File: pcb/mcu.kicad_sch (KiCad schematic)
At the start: 24 parts, among them SW1 PTS815, SW3 PTS815, U8 STM32H523VETx, Y1 ECS-160-12-33B2Q-JES-TR3, Y2 SC32S-7PF20PPM

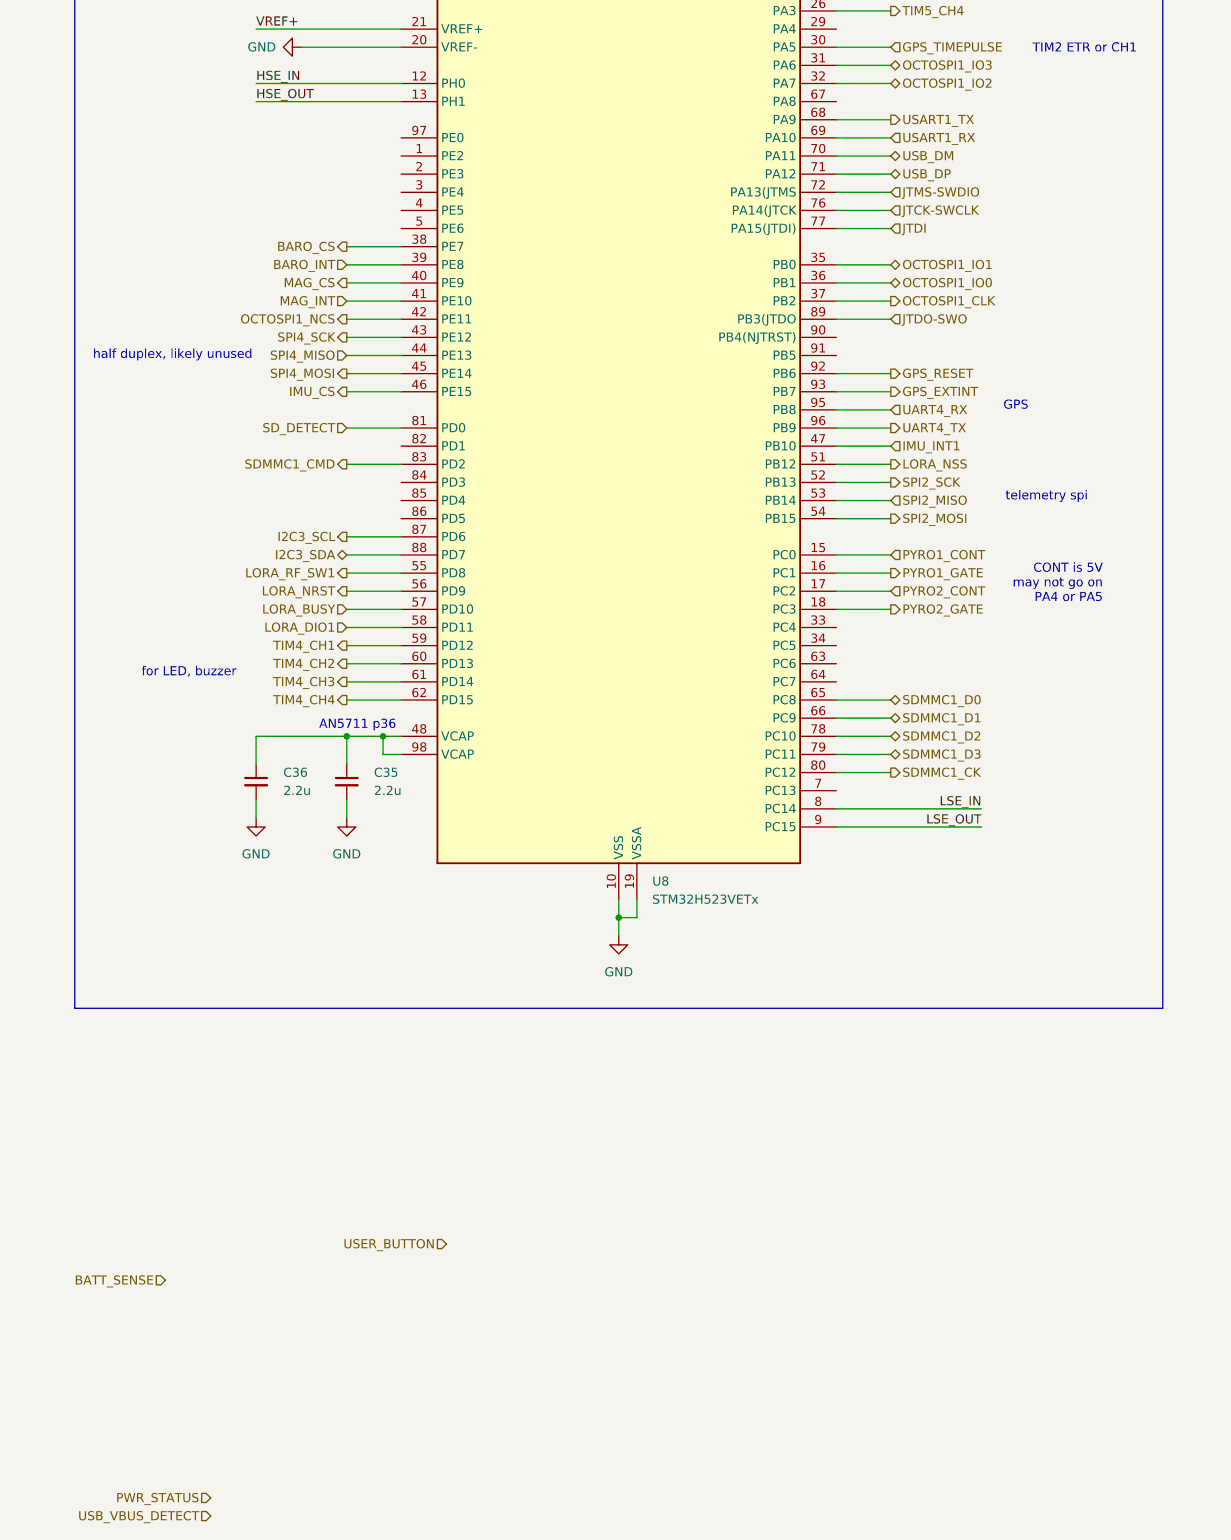
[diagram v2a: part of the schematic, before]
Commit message: Shuffle pins to allow for additional I2C
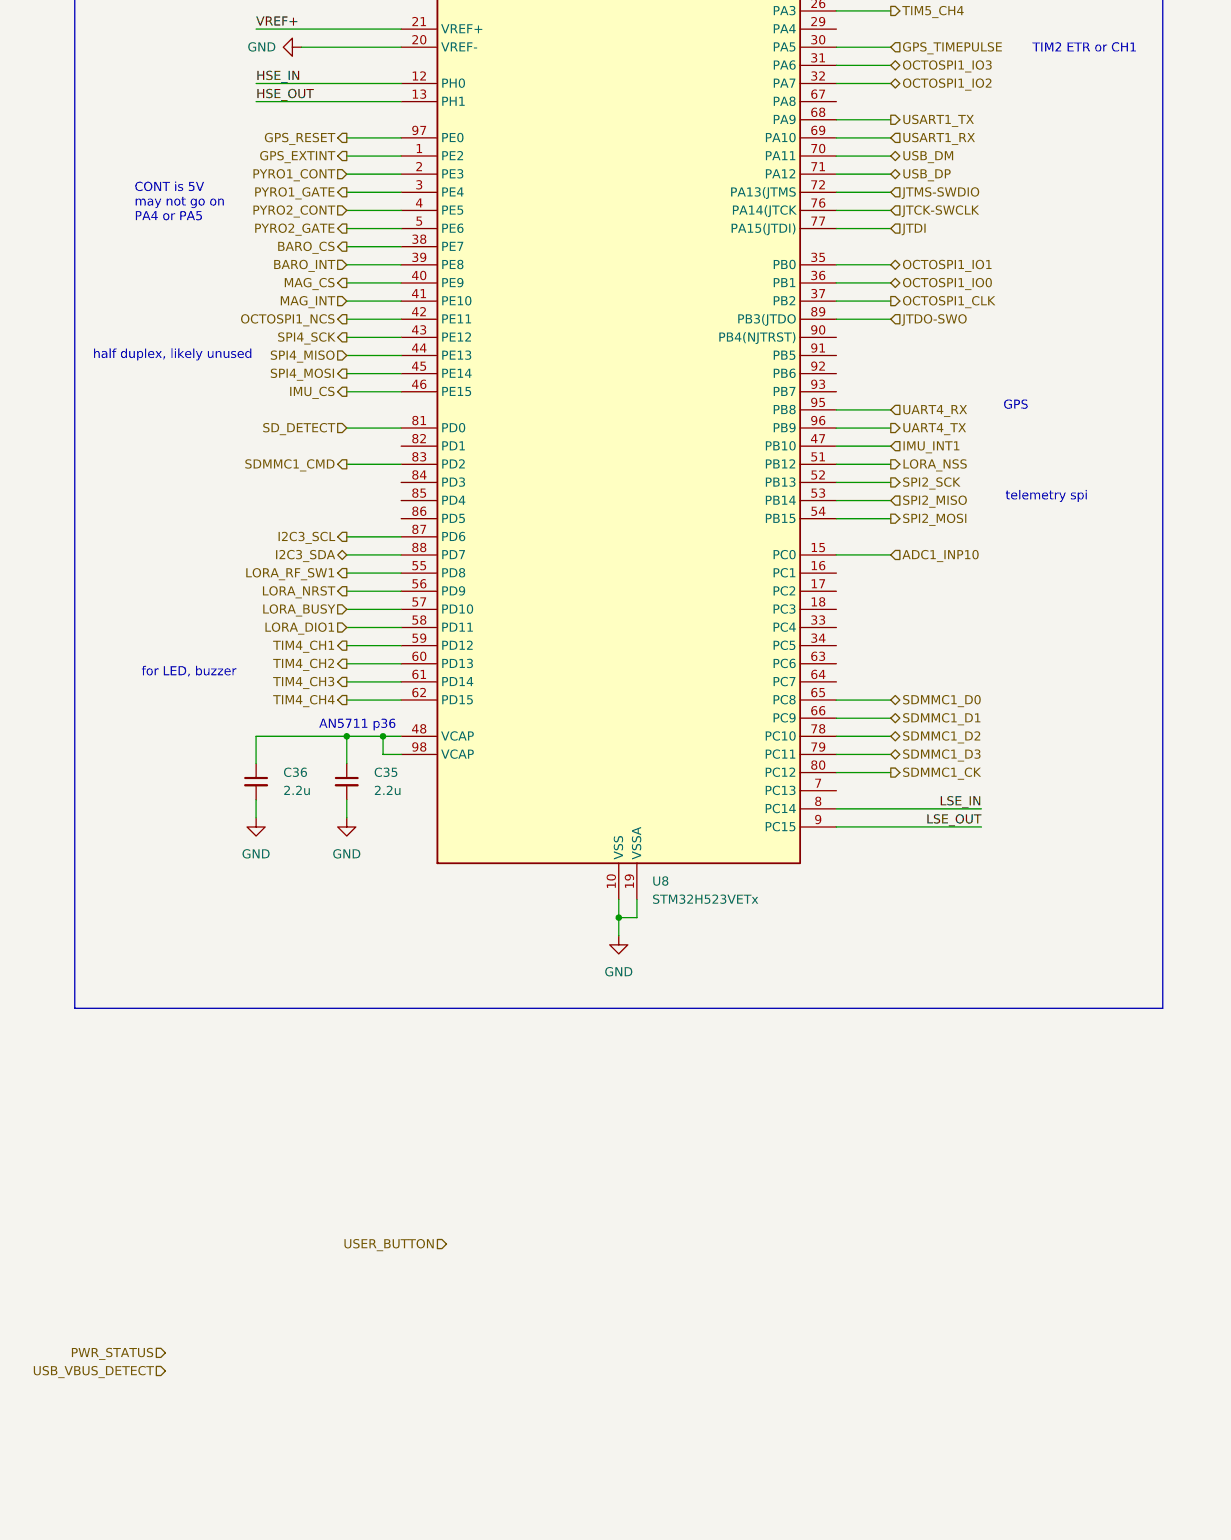
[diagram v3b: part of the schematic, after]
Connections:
- net GPS_EXTINT: now also U8.1 (PE2); no longer U8.93 (PB7)
- net GPS_RESET: now also U8.97 (PE0); no longer U8.92 (PB6)
- net PYRO1_CONT: now also U8.2 (PE3); no longer U8.15 (PC0)
- net PYRO1_GATE: now also U8.3 (PE4); no longer U8.16 (PC1)
- net PYRO2_CONT: now also U8.4 (PE5); no longer U8.17 (PC2)
- net PYRO2_GATE: now also U8.5 (PE6); no longer U8.18 (PC3)
- new net ADC1_INP10: U8.15 (PC0)

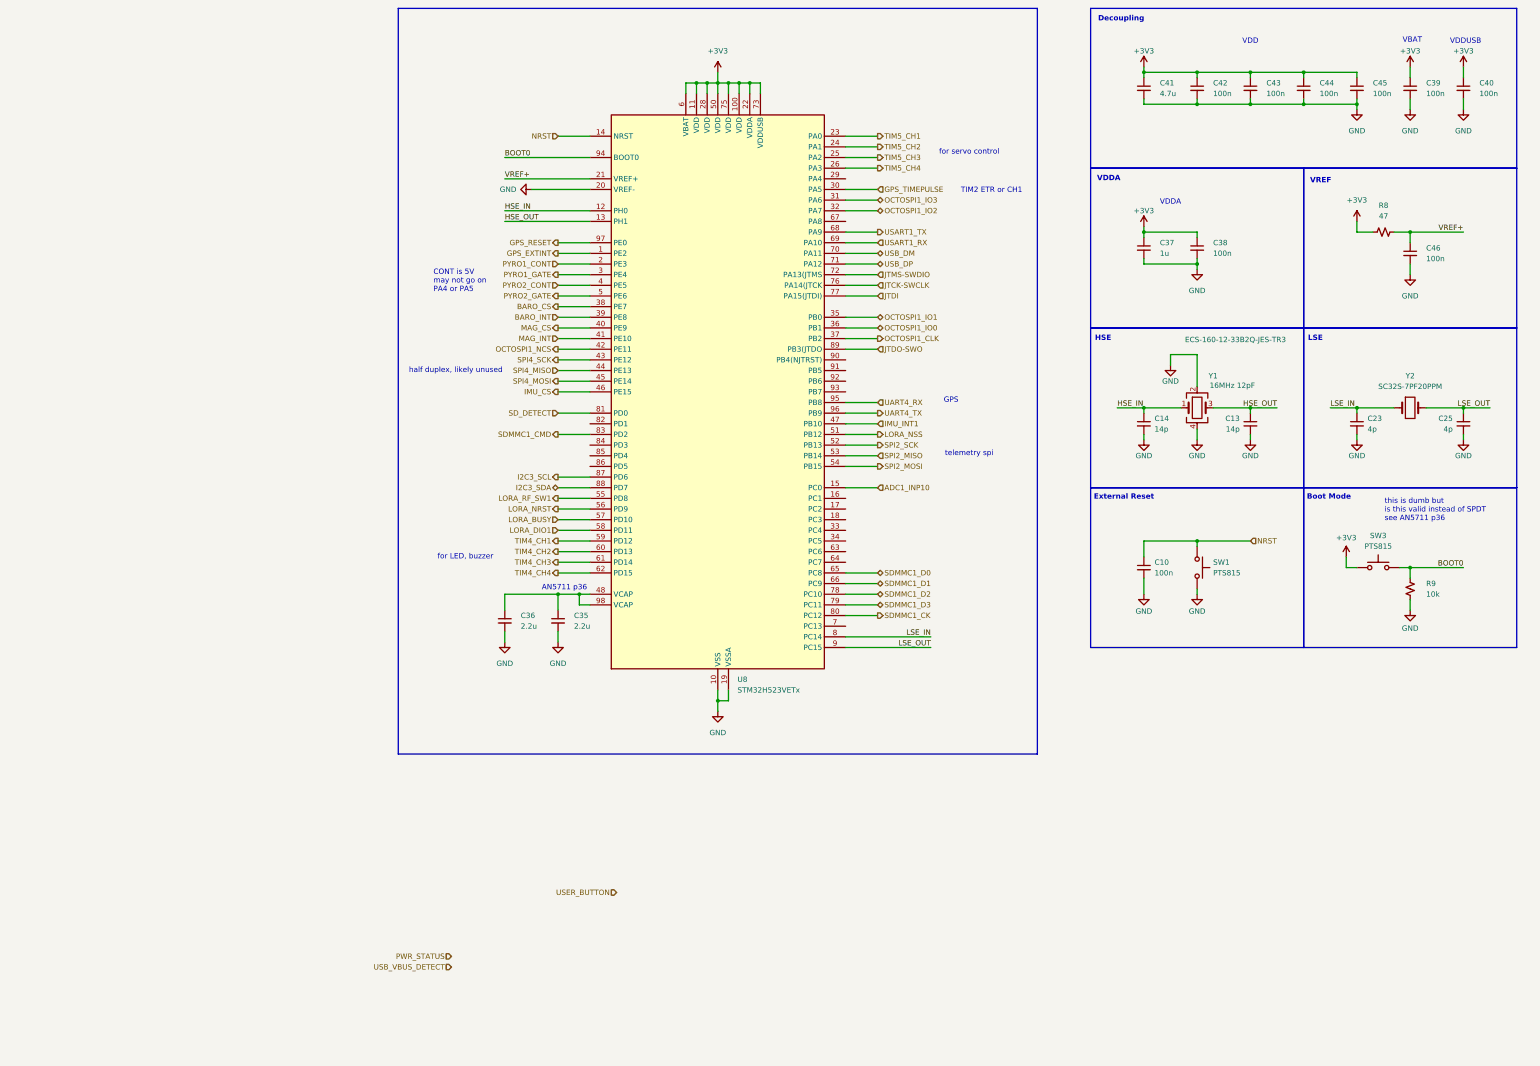
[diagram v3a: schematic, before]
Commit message: Fix pin directionality
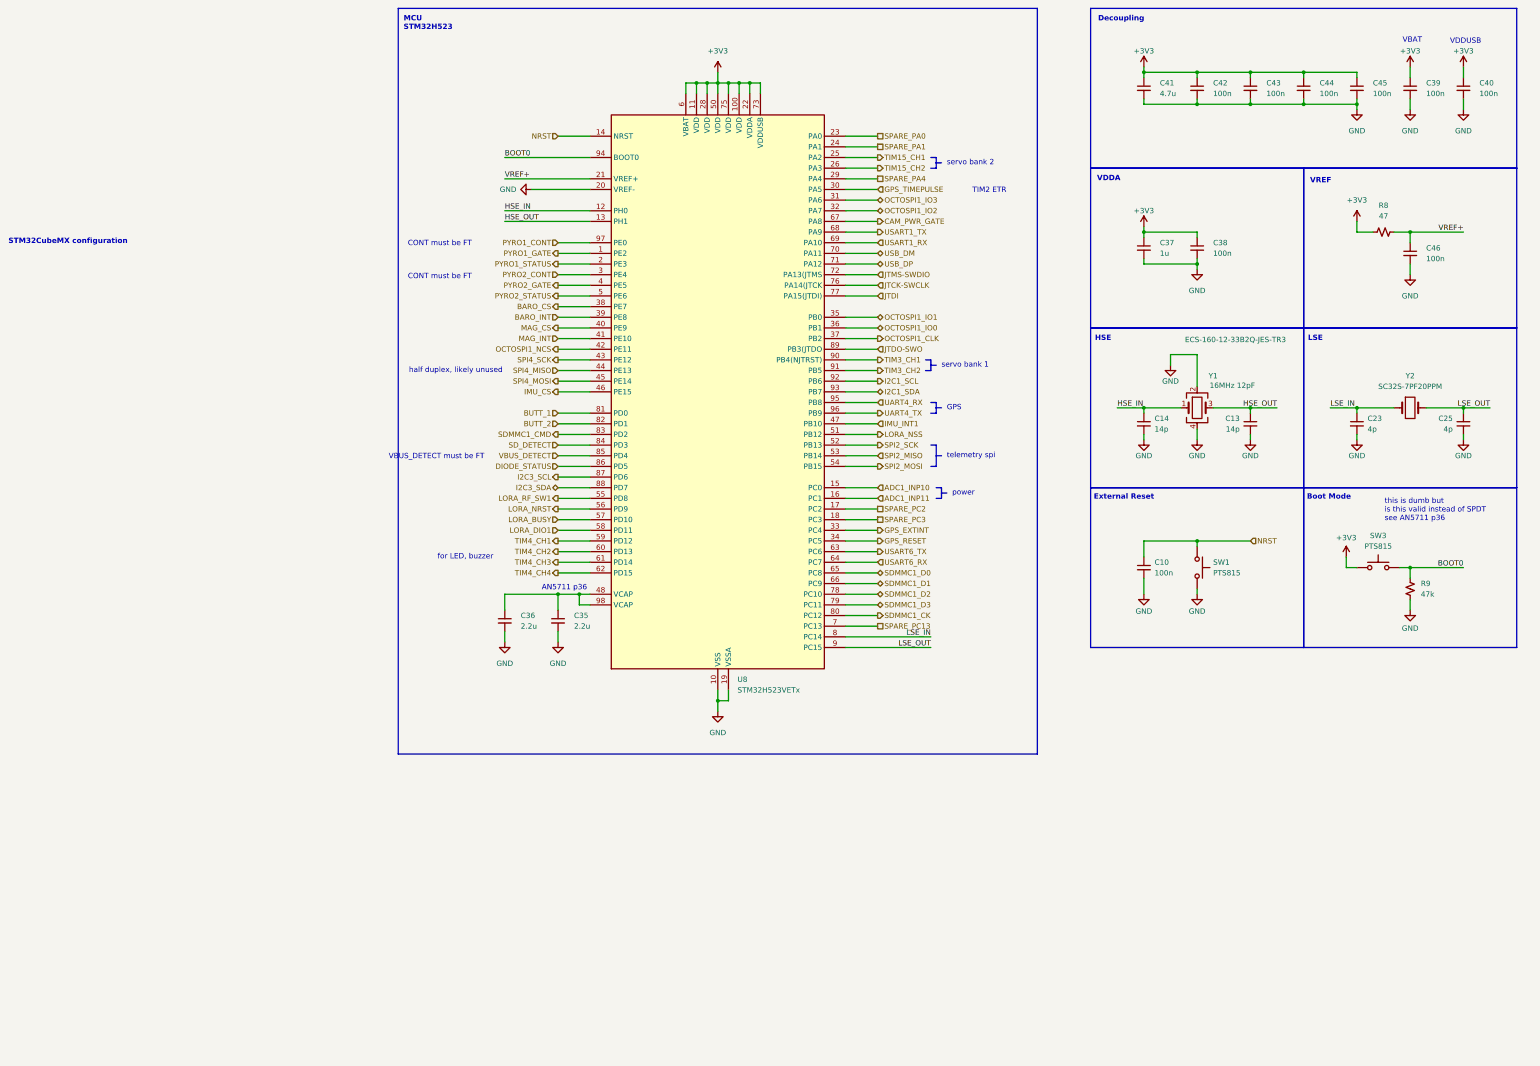
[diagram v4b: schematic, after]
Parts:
- R9: value 10k -> 47k
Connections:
- net GPS_EXTINT: now also U8.33 (PC4); no longer U8.1 (PE2)
- net GPS_RESET: now also U8.34 (PC5); no longer U8.97 (PE0)
- net PYRO1_CONT: now also U8.97 (PE0); no longer U8.2 (PE3)
- net PYRO1_GATE: now also U8.1 (PE2); no longer U8.3 (PE4)
- net PYRO2_CONT: now also U8.3 (PE4); no longer U8.4 (PE5)
- net PYRO2_GATE: now also U8.4 (PE5); no longer U8.5 (PE6)
- net SD_DETECT: now also U8.84 (PD3); no longer U8.81 (PD0)
- net ADC1_INP11: now reaches U8.16 (PC1)
- net SPARE_PC2: now reaches U8.17 (PC2)
- net SPARE_PC3: now reaches U8.18 (PC3)
- net SPARE_PA4: now reaches U8.29 (PA4)
- net USART6_TX: now reaches U8.63 (PC6)
- net USART6_RX: now reaches U8.64 (PC7)
- net CAM_PWR_GATE: now reaches U8.67 (PA8)
- net SPARE_PC13: now reaches U8.7 (PC13)
- net BUTT_2: now reaches U8.82 (PD1)
- net VBUS_DETECT: now reaches U8.85 (PD4)
- net DIODE_STATUS: now reaches U8.86 (PD5)
- net TIM3_CH1: now reaches U8.90 (PB4(NJTRST))
- net TIM3_CH2: now reaches U8.91 (PB5)
- net I2C1_SCL: now reaches U8.92 (PB6)
- net I2C1_SDA: now reaches U8.93 (PB7)
- net TIM5_CH1 renamed SPARE_PA0
- net TIM5_CH2 renamed SPARE_PA1
- net TIM5_CH3 renamed TIM15_CH1
- net TIM5_CH4 renamed TIM15_CH2
- new net BUTT_1: U8.81 (PD0)
- new net PYRO1_STATUS: U8.2 (PE3)
- new net PYRO2_STATUS: U8.5 (PE6)
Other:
- note added: "CONT must be FT"
- note added: "MCU STM32H523"
- note added: "STM32CubeMX configuration"
- note added: "TIM2 ETR"
- note added: "VBUS_DETECT must be FT"
- note added: "power"
- note added: "servo bank 1"
- note added: "servo bank 2"
- note removed: "CONT is 5V may not go on PA4 or PA5"
- note removed: "TIM2 ETR or CH1"
- note removed: "VDD"
- note removed: "for servo control"

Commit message: Assign most footprints
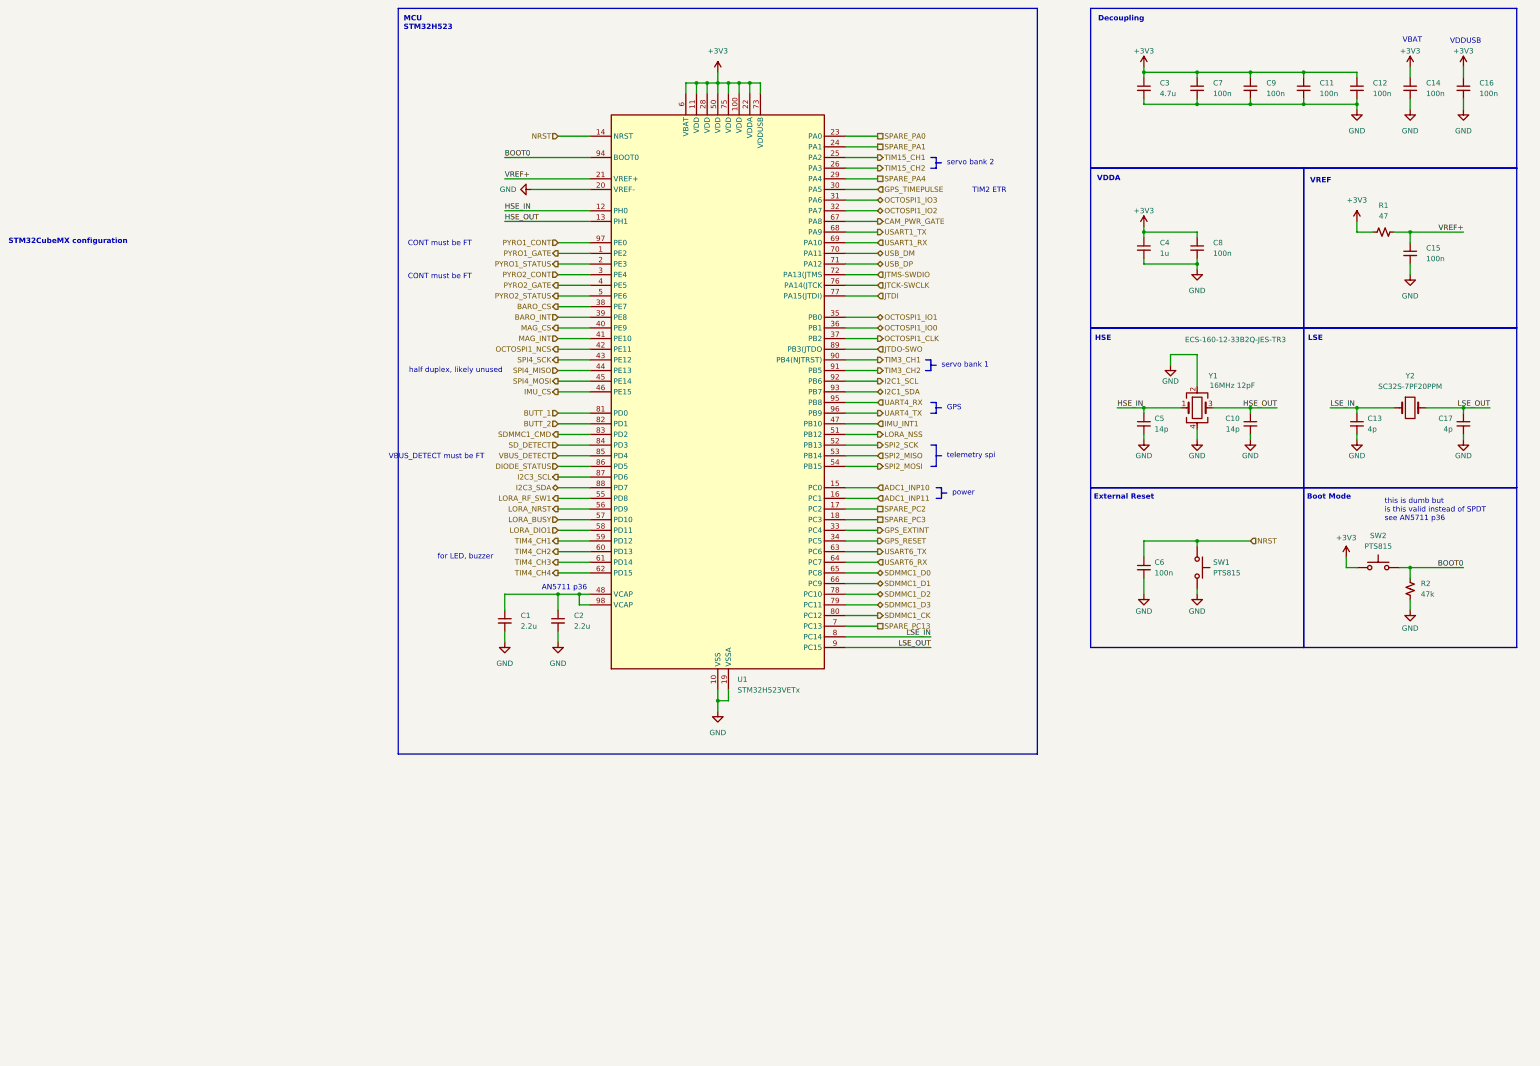
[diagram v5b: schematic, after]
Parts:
- C1: renamed from C36; footprint (none) -> Capacitor_SMD:C_0603_1608Metric
- C10: renamed from C13; footprint (none) -> Capacitor_SMD:C_0603_1608Metric
- C11: renamed from C44; footprint (none) -> Capacitor_SMD:C_0603_1608Metric
- C12: renamed from C45; footprint (none) -> Capacitor_SMD:C_0603_1608Metric
- C13: renamed from C23; footprint (none) -> Capacitor_SMD:C_0603_1608Metric
- C14: renamed from C39; footprint (none) -> Capacitor_SMD:C_0603_1608Metric
- C15: renamed from C46; footprint (none) -> Capacitor_SMD:C_0603_1608Metric
- C16: renamed from C40; footprint (none) -> Capacitor_SMD:C_0603_1608Metric
- C17: renamed from C25; footprint (none) -> Capacitor_SMD:C_0603_1608Metric
- C2: renamed from C35; footprint (none) -> Capacitor_SMD:C_0603_1608Metric
- C3: renamed from C41; footprint (none) -> Capacitor_SMD:C_0603_1608Metric
- C4: renamed from C37; footprint (none) -> Capacitor_SMD:C_0603_1608Metric
- C5: renamed from C14; footprint (none) -> Capacitor_SMD:C_0603_1608Metric
- C6: renamed from C10; footprint (none) -> Capacitor_SMD:C_0603_1608Metric
- C7: renamed from C42; footprint (none) -> Capacitor_SMD:C_0603_1608Metric
- C8: renamed from C38; footprint (none) -> Capacitor_SMD:C_0603_1608Metric
- C9: renamed from C43; footprint (none) -> Capacitor_SMD:C_0603_1608Metric
- R1: renamed from R8; footprint (none) -> Resistor_SMD:R_0603_1608Metric
- R2: renamed from R9; footprint (none) -> Resistor_SMD:R_0603_1608Metric
- SW1: footprint (none) -> PTS815_SJM_250_SMTR_LFS:SW_Push_PTS815_SJM_250_SMTR_LFS
- SW2: renamed from SW3; footprint (none) -> PTS815_SJM_250_SMTR_LFS:SW_Push_PTS815_SJM_250_SMTR_LFS
- Y2: footprint (none) -> Crystal:Crystal_SMD_3215-2Pin_3.2x1.5mm
- renumbered U8 to U1
